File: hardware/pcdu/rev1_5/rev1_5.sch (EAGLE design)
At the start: 11 parts, among them IC1 74HC595N, X1 MUSBV, X2 MUSBV, X3 MUSBV, X4 MUSBV, X7 22-23-2041, X8 22-23-2041

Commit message: Added PCU board, updated revision 5 PDU board
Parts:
- removed X6: (no value), con-wago-500:W237-102
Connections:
- net GND: no longer X6-2.KL
- net VCC: no longer X6-1.KL
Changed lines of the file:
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@@
 <part name="U$2" library="FDC6305N" deviceset="FDC6305N" device=""/>
 <part name="X5" library="con-wago-500" deviceset="W237-102" device=""/>
-<part name="X6" library="con-wago-500" deviceset="W237-102" device=""/>
 <part name="X7" library="con-molex" deviceset="22-23-2041" device=""/>
 <part name="X8" library="con-molex" deviceset="22-23-2041" device=""/>
@@
 <instance part="X5" gate="-1" x="30.48" y="15.24"/>
 <instance part="X5" gate="-2" x="30.48" y="10.16"/>
-<instance part="X6" gate="-1" x="30.48" y="2.54"/>
-<instance part="X6" gate="-2" x="30.48" y="-2.54"/>
 <instance part="X7" gate="-1" x="33.02" y="-12.7" rot="MR0"/>
 <instance part="X7" gate="-2" x="33.02" y="-15.24" rot="MR0"/>
@@
 <wire x1="35.56" y1="15.24" x2="38.1" y2="15.24" width="0.1524" layer="91"/>
 <label x="38.1" y="15.24" size="1.778" layer="95"/>
-</segment>
-<segment>
-<pinref part="X6" gate="-1" pin="KL"/>
-<wire x1="35.56" y1="2.54" x2="38.1" y2="2.54" width="0.1524" layer="91"/>
-<label x="38.1" y="2.54" size="1.778" layer="95"/>
 </segment>
 <segment>
@@
 </segment>
 <segment>
-<pinref part="X6" gate="-2" pin="KL"/>
-<wire x1="35.56" y1="-2.54" x2="38.1" y2="-2.54" width="0.1524" layer="91"/>
-<label x="38.1" y="-2.54" size="1.778" layer="95"/>
-</segment>
-<segment>

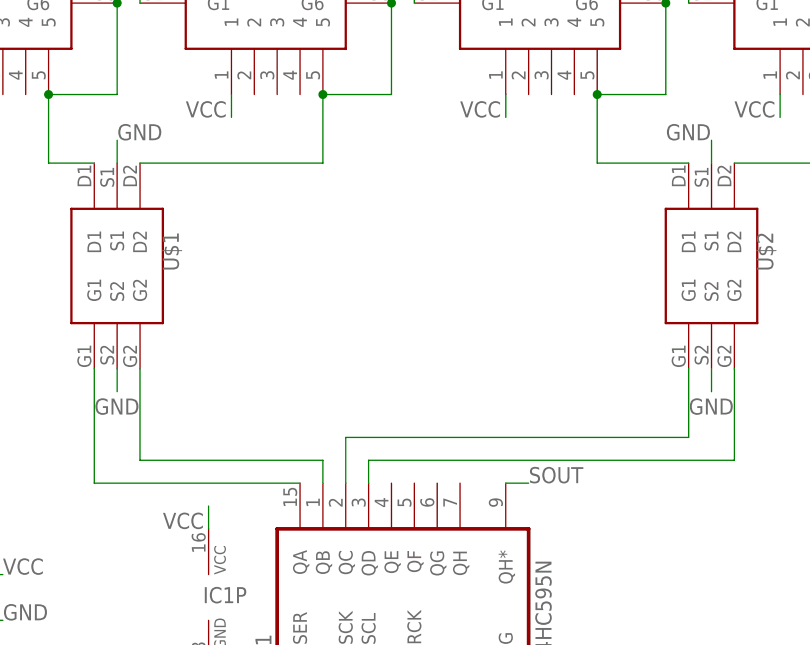
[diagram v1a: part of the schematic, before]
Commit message: Added software controlled LED indicators to rev1_5
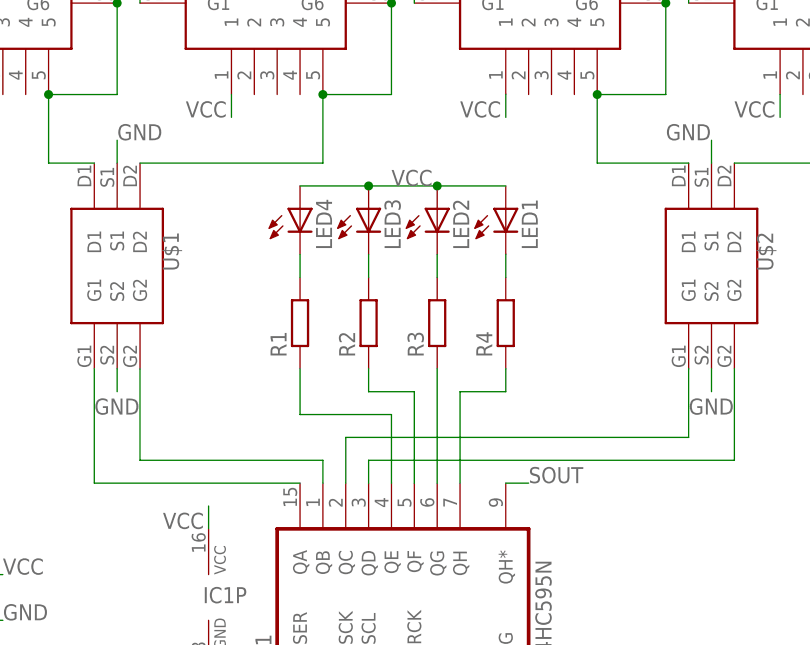
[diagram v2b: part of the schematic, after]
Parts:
- added LED1, LED2, LED3, LED4: (no value), eagle-ltspice:LED_E
- added R1, R2, R3, R4: (no value), eagle-ltspice:RR1005
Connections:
- new net N$13: IC1A.QE, R1.1
- new net N$14: IC1A.QF, R2.1
- new net N$15: IC1A.QG, R3.1
- new net N$16: IC1A.QH, R4.1
- new net N$5: LED4.C, R1.2
- new net N$6: LED3.C, R2.2
- new net N$7: LED2.C, R3.2
- new net N$8: LED1.C, R4.2
- net VCC: now also LED1.A, LED2.A, LED3.A, LED4.A
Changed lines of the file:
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@@
 <?xml version="1.0" encoding="utf-8"?>
 <!DOCTYPE eagle SYSTEM "eagle.dtd">
-<eagle version="7.6.0">
+<eagle version="7.7.0">
 <drawing>
 <settings>
@@
 <layer number="97" name="Info" color="7" fill="1" visible="yes" active="yes"/>
 <layer number="98" name="Guide" color="6" fill="1" visible="yes" active="yes"/>
+<layer number="99" name="SpiceOrder" color="5" fill="1" visible="yes" active="yes"/>
 </layers>
 <schematic xreflabel="%F%N/%S.%C%R" xrefpart="/%S.%C%R">
@@
 <part name="X3" library="MUSBV" deviceset="MUSBV" device=""/>
 <part name="X4" library="MUSBV" deviceset="MUSBV" device=""/>
+<part name="LED1" library="eagle-ltspice" deviceset="LED_E" device=""/>
+<part name="LED2" library="eagle-ltspice" deviceset="LED_E" device=""/>
+<part name="LED3" library="eagle-ltspice" deviceset="LED_E" device=""/>
+<part name="LED4" library="eagle-ltspice" deviceset="LED_E" device=""/>
+<part name="R1" library="eagle-ltspice" deviceset="R" device="R1005"/>
+<part name="R2" library="eagle-ltspice" deviceset="R" device="R1005"/>
+<part name="R3" library="eagle-ltspice" deviceset="R" device="R1005"/>
+<part name="R4" library="eagle-ltspice" deviceset="R" device="R1005"/>
 </parts>
 <sheets>
@@
 <instance part="X3" gate="G$1" x="96.52" y="76.2"/>
 <instance part="X4" gate="G$1" x="127" y="76.2"/>
+<instance part="LED1" gate="G$1" x="93.98" y="55.88"/>
+<instance part="LED2" gate="G$1" x="86.36" y="55.88"/>
+<instance part="LED3" gate="G$1" x="78.74" y="55.88"/>
+<instance part="LED4" gate="G$1" x="71.12" y="55.88"/>
+<instance part="R1" gate="G$1" x="71.12" y="43.18" rot="R90"/>
+<instance part="R2" gate="G$1" x="78.74" y="43.18" rot="R90"/>
+<instance part="R3" gate="G$1" x="86.36" y="43.18" rot="R90"/>
+<instance part="R4" gate="G$1" x="93.98" y="43.18" rot="R90"/>
 </instances>
 <busses>
@@
 <wire x1="124.46" y1="68.58" x2="124.46" y2="66.04" width="0.1524" layer="91"/>
 <label x="119.38" y="66.04" size="1.778" layer="95"/>
+</segment>
+<segment>
+<pinref part="LED4" gate="G$1" pin="A"/>
+<pinref part="LED3" gate="G$1" pin="A"/>
+<wire x1="71.12" y1="58.42" x2="78.74" y2="58.42" width="0.1524" layer="91"/>
+<pinref part="LED2" gate="G$1" pin="A"/>
+<wire x1="78.74" y1="58.42" x2="86.36" y2="58.42" width="0.1524" layer="91"/>
+<junction x="78.74" y="58.42"/>
+<pinref part="LED1" gate="G$1" pin="A"/>
+<wire x1="86.36" y1="58.42" x2="93.98" y2="58.42" width="0.1524" layer="91"/>
+<junction x="86.36" y="58.42"/>
+<label x="81.28" y="58.42" size="1.778" layer="95"/>
 </segment>
 </net>
@@
 </segment>
 </net>
+<net name="N$13" class="0">
+<segment>
+<pinref part="IC1" gate="A" pin="QE"/>
+<wire x1="81.28" y1="33.02" x2="81.28" y2="25.4" width="0.1524" layer="91"/>
+<wire x1="81.28" y1="33.02" x2="71.12" y2="33.02" width="0.1524" layer="91"/>
+<wire x1="71.12" y1="33.02" x2="71.12" y2="38.1" width="0.1524" layer="91"/>
+<pinref part="R1" gate="G$1" pin="1"/>
+</segment>
+</net>
+<net name="N$14" class="0">
+<segment>
+<pinref part="IC1" gate="A" pin="QF"/>
+<wire x1="83.82" y1="25.4" x2="83.82" y2="35.56" width="0.1524" layer="91"/>
+<wire x1="83.82" y1="35.56" x2="78.74" y2="35.56" width="0.1524" layer="91"/>
+<wire x1="78.74" y1="35.56" x2="78.74" y2="38.1" width="0.1524" layer="91"/>
+<pinref part="R2" gate="G$1" pin="1"/>
+</segment>
+</net>
+<net name="N$15" class="0">
+<segment>
+<pinref part="IC1" gate="A" pin="QG"/>
+<wire x1="86.36" y1="25.4" x2="86.36" y2="38.1" width="0.1524" layer="91"/>
+<pinref part="R3" gate="G$1" pin="1"/>
+</segment>
+</net>
+<net name="N$16" class="0">
+<segment>
+<pinref part="IC1" gate="A" pin="QH"/>
+<wire x1="88.9" y1="25.4" x2="88.9" y2="35.56" width="0.1524" layer="91"/>
+<wire x1="88.9" y1="35.56" x2="93.98" y2="35.56" width="0.1524" layer="91"/>
+<wire x1="93.98" y1="35.56" x2="93.98" y2="38.1" width="0.1524" layer="91"/>
+<pinref part="R4" gate="G$1" pin="1"/>
+</segment>
+</net>
+<net name="N$5" class="0">
+<segment>
+<pinref part="LED4" gate="G$1" pin="C"/>
+<pinref part="R1" gate="G$1" pin="2"/>
+<wire x1="71.12" y1="50.8" x2="71.12" y2="48.26" width="0.1524" layer="91"/>
+</segment>
+</net>
+<net name="N$6" class="0">
+<segment>
+<pinref part="LED3" gate="G$1" pin="C"/>
+<pinref part="R2" gate="G$1" pin="2"/>
+<wire x1="78.74" y1="50.8" x2="78.74" y2="48.26" width="0.1524" layer="91"/>
+</segment>
+</net>
+<net name="N$7" class="0">
+<segment>
+<pinref part="LED2" gate="G$1" pin="C"/>
+<pinref part="R3" gate="G$1" pin="2"/>
+<wire x1="86.36" y1="50.8" x2="86.36" y2="48.26" width="0.1524" layer="91"/>
+</segment>
+</net>
+<net name="N$8" class="0">
+<segment>
+<pinref part="LED1" gate="G$1" pin="C"/>
+<pinref part="R4" gate="G$1" pin="2"/>
+<wire x1="93.98" y1="50.8" x2="93.98" y2="48.26" width="0.1524" layer="91"/>
+</segment>
+</net>
